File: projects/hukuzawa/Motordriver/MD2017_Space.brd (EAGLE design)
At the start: 70 x 70 mm, 7 parts

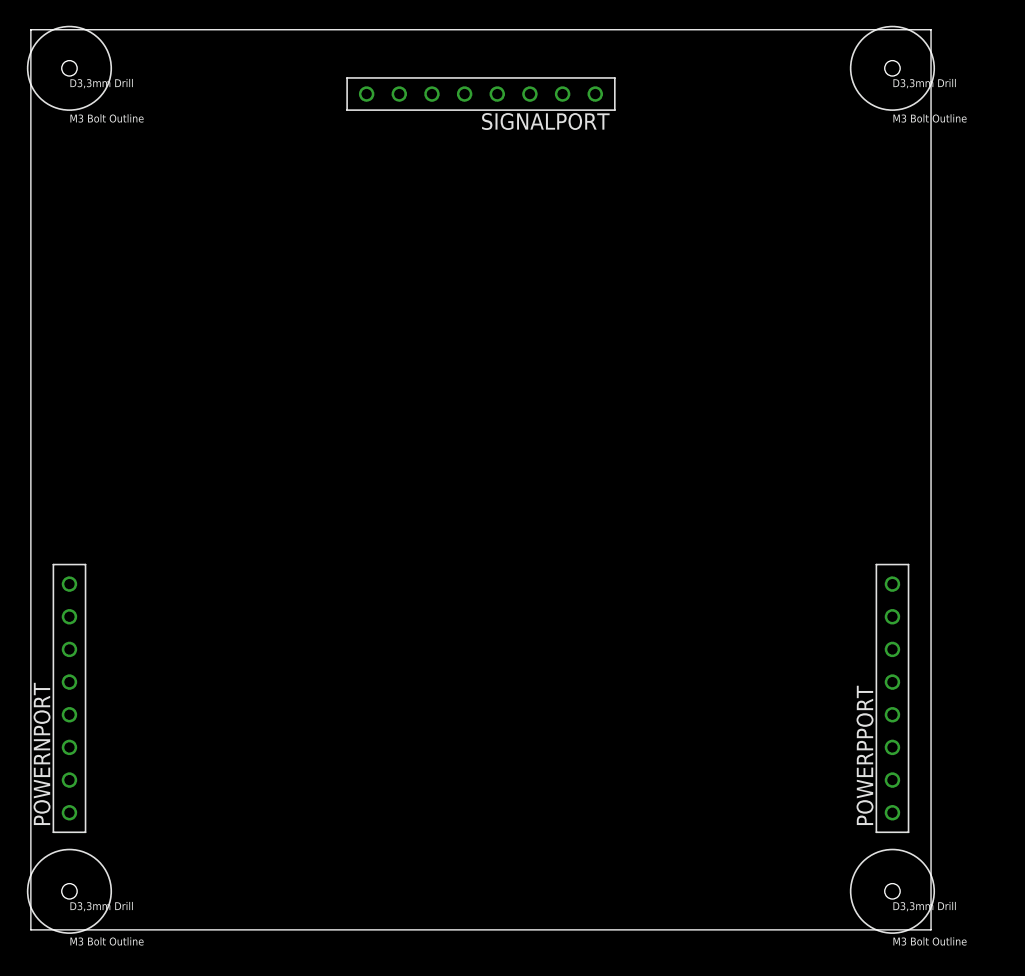
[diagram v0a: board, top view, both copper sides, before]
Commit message: モータードライバ全ボード図完成
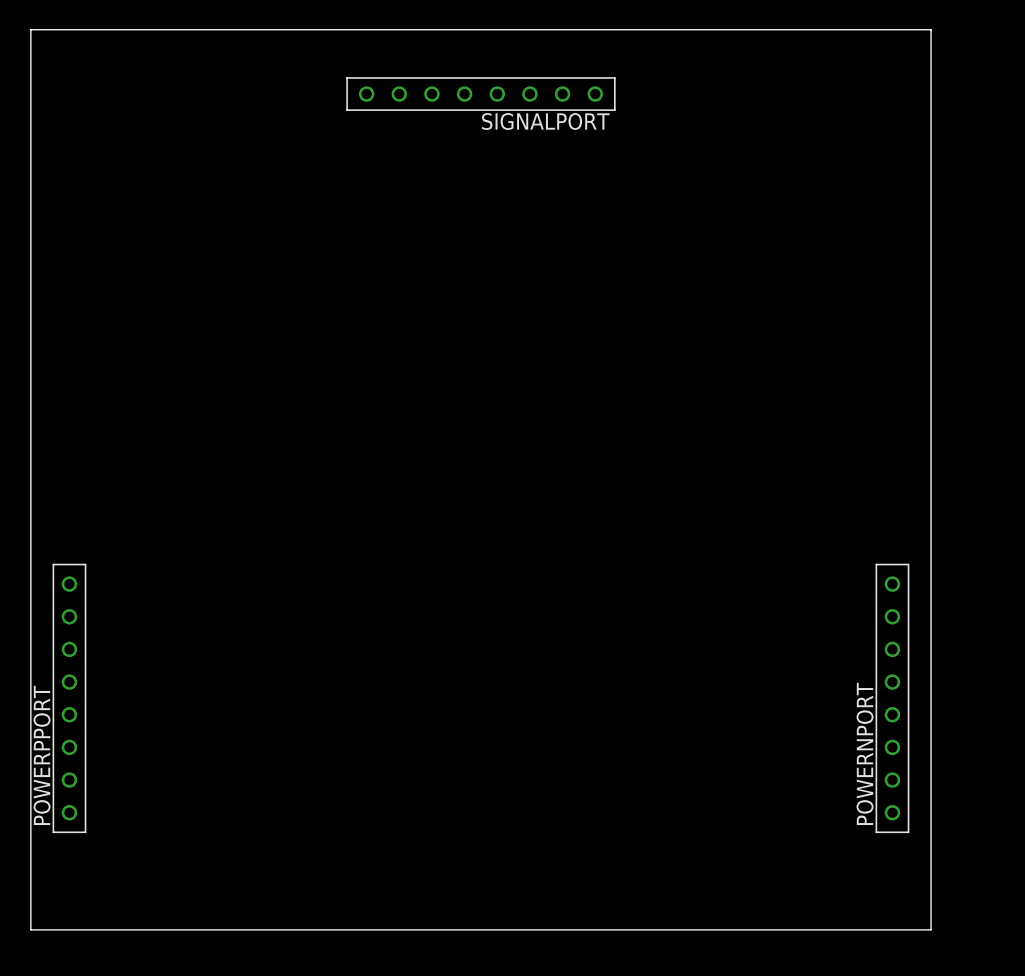
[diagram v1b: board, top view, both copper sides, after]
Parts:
- removed H1, H2, H3, H4: HOLE3.3M3BOLT, FP-21T for MITS:HOLE3.3
- moved POWERNPORT 64.0 mm to (67.0, 18.0)
- moved POWERPPORT 64.0 mm to (3.00, 18.0)
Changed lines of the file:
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@@
 <layer number="43" name="vRestrict" color="2" fill="10" visible="yes" active="yes"/>
 <layer number="44" name="Drills" color="7" fill="1" visible="no" active="yes"/>
-<layer number="45" name="Holes" color="7" fill="1" visible="no" active="yes"/>
+<layer number="45" name="Holes" color="7" fill="1" visible="yes" active="yes"/>
 <layer number="46" name="Milling" color="3" fill="1" visible="no" active="yes"/>
 <layer number="47" name="Measures" color="7" fill="1" visible="no" active="yes"/>
 <layer number="48" name="Document" color="7" fill="1" visible="yes" active="yes"/>
 <layer number="49" name="Reference" color="7" fill="1" visible="yes" active="yes"/>
-<layer number="50" name="dxf" color="7" fill="1" visible="no" active="no"/>
 <layer number="51" name="tDocu" color="7" fill="1" visible="yes" active="yes"/>
 <layer number="52" name="bDocu" color="7" fill="1" visible="yes" active="yes"/>
@@
 <layer number="97" name="Info" color="7" fill="1" visible="no" active="no"/>
 <layer number="98" name="Guide" color="6" fill="1" visible="no" active="no"/>
-<layer number="101" name="Patch_Top" color="12" fill="4" visible="yes" active="yes"/>
-<layer number="116" name="Patch_BOT" color="9" fill="4" visible="yes" active="yes"/>
-<layer number="121" name="_tplace" color="14" fill="1" visible="yes" active="yes"/>
-<layer number="122" name="_bplace" color="14" fill="1" visible="yes" active="yes"/>
-<layer number="250" name="Descript" color="3" fill="1" visible="no" active="no"/>
-<layer number="251" name="SMDround" color="12" fill="11" visible="no" active="no"/>
 </layers>
 <board>
@@
 <wire x1="70" y1="70" x2="0" y2="70" width="0" layer="20"/>
 <wire x1="0" y1="70" x2="0" y2="0" width="0" layer="20"/>
+<rectangle x1="23" y1="5" x2="58.5" y2="38" layer="45"/>
 </plain>
 <attributes>
@@
 <elements>
 <element name="SIGNALPORT" library="FH105" package="FH105-1X8SG" value="8PIN" x="35" y="65" rot="R180"/>
-<element name="POWERPPORT" library="FH105" package="FH105-1X8SG" value="8PIN" x="67" y="18" rot="R90"/>
-<element name="POWERNPORT" library="FH105" package="FH105-1X8SG" value="8PIN" x="3" y="18" rot="R90"/>
-<element name="H1" library="FP-21T for MITS" package="HOLE3.3" value="HOLE3.3M3BOLT" x="67" y="3"/>
-<element name="H2" library="FP-21T for MITS" package="HOLE3.3" value="HOLE3.3M3BOLT" x="3" y="3"/>
-<element name="H3" library="FP-21T for MITS" package="HOLE3.3" value="HOLE3.3M3BOLT" x="67" y="67"/>
-<element name="H4" library="FP-21T for MITS" package="HOLE3.3" value="HOLE3.3M3BOLT" x="3" y="67"/>
+<element name="POWERPPORT" library="FH105" package="FH105-1X8SG" value="8PIN" x="3" y="18" rot="R90"/>
+<element name="POWERNPORT" library="FH105" package="FH105-1X8SG" value="8PIN" x="67" y="18" rot="R90"/>
 </elements>
 <signals>

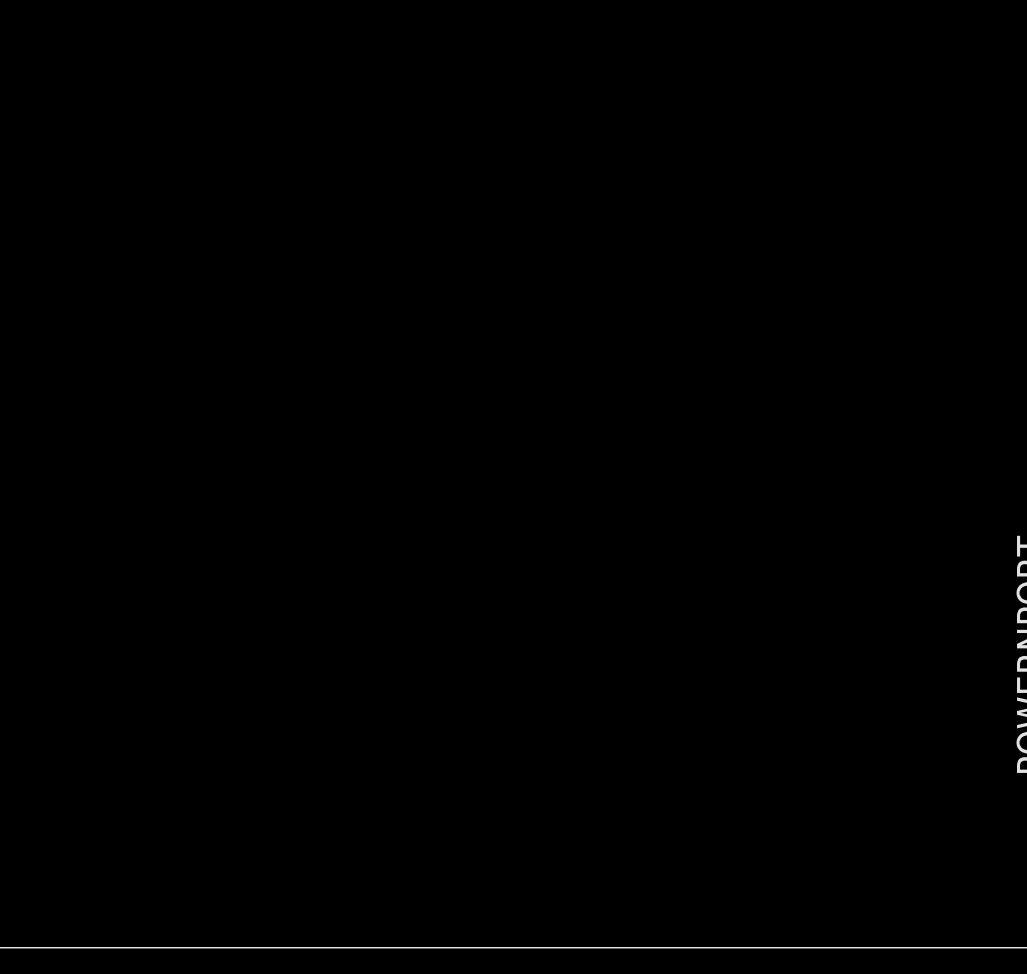
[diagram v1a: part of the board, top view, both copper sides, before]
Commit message: モータードライバデータ修正
ドリル径の修正、それに伴う配置の若干の変更
ダイオードのライブラリの修正
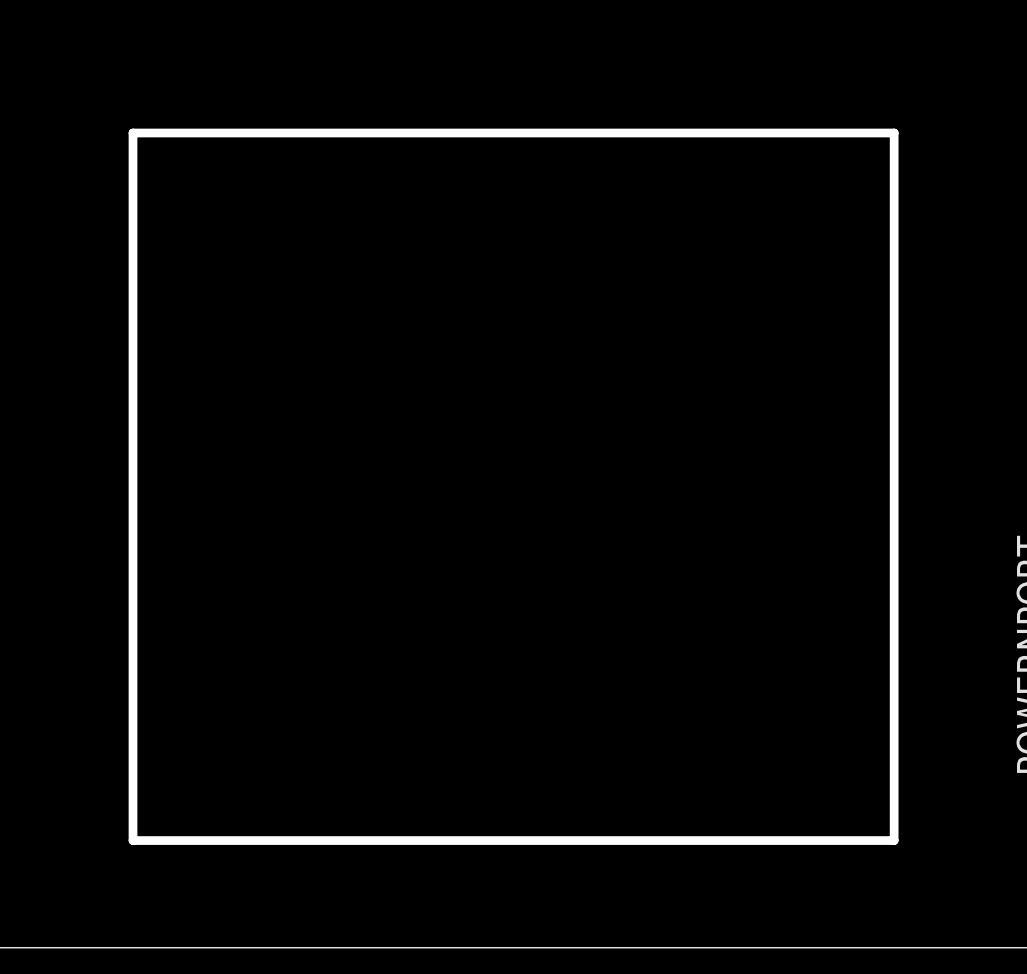
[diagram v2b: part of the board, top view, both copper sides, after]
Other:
- outline, holes or cut-outs redrawn
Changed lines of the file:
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@@
 <wire x1="70" y1="70" x2="0" y2="70" width="0" layer="20"/>
 <wire x1="0" y1="70" x2="0" y2="0" width="0" layer="20"/>
-<rectangle x1="23" y1="5" x2="58.5" y2="38" layer="45"/>
+<wire x1="23" y1="38" x2="23" y2="5" width="0.4064" layer="20"/>
+<wire x1="23" y1="5" x2="58.5" y2="5" width="0.4064" layer="20"/>
+<wire x1="58.5" y1="5" x2="58.5" y2="38" width="0.4064" layer="20"/>
+<wire x1="58.5" y1="38" x2="23" y2="38" width="0.4064" layer="20"/>
 </plain>
 <attributes>

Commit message: モータードライバ修正
穴径を1.0～1.2mmの範囲に収まるよう修正
Dimensionラインの太さを0に修正
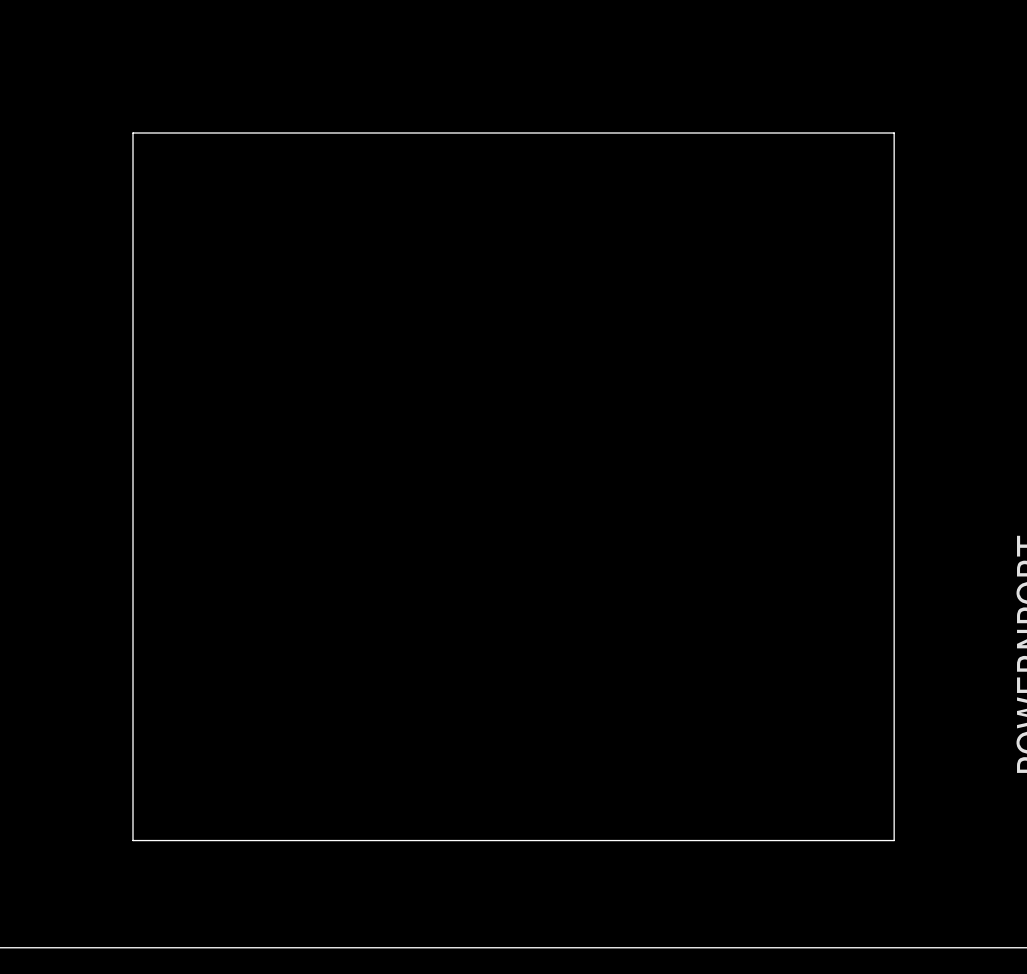
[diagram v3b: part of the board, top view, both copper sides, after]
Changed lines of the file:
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@@
 <wire x1="70" y1="70" x2="0" y2="70" width="0" layer="20"/>
 <wire x1="0" y1="70" x2="0" y2="0" width="0" layer="20"/>
-<wire x1="23" y1="38" x2="23" y2="5" width="0.4064" layer="20"/>
-<wire x1="23" y1="5" x2="58.5" y2="5" width="0.4064" layer="20"/>
-<wire x1="58.5" y1="5" x2="58.5" y2="38" width="0.4064" layer="20"/>
-<wire x1="58.5" y1="38" x2="23" y2="38" width="0.4064" layer="20"/>
+<wire x1="23" y1="38" x2="23" y2="5" width="0" layer="20"/>
+<wire x1="23" y1="5" x2="58.5" y2="5" width="0" layer="20"/>
+<wire x1="58.5" y1="5" x2="58.5" y2="38" width="0" layer="20"/>
+<wire x1="58.5" y1="38" x2="23" y2="38" width="0" layer="20"/>
 </plain>
 <attributes>
